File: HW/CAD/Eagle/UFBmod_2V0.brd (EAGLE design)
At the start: 98.4 x 89.5 mm, 93 parts, among them T0551 MMBT2222, U0501 MIDAS_MCCOG21605B6W-FPTLWI, U0601 MAX5217, U0701 AT86RF215-ZU, U0711 ASVTX-13-D-26.000MHZ-I05-T, U0811 PE4259, U0821 RFX1010, U0881 B39871B3440U410, X0891 ANTENNATINY, X0895 ANTENNATINY, X1011 TTE_EN11-HSM, X1211 MOLEX 105017-0001, X1221 PHOENIX_1990067_1X8X2MM50_PTS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, X1222 PHOENIX_1990067_1X8X2MM50_PTS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, X1223 PHOENIX_1990067_1X8X2MM50_PTS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

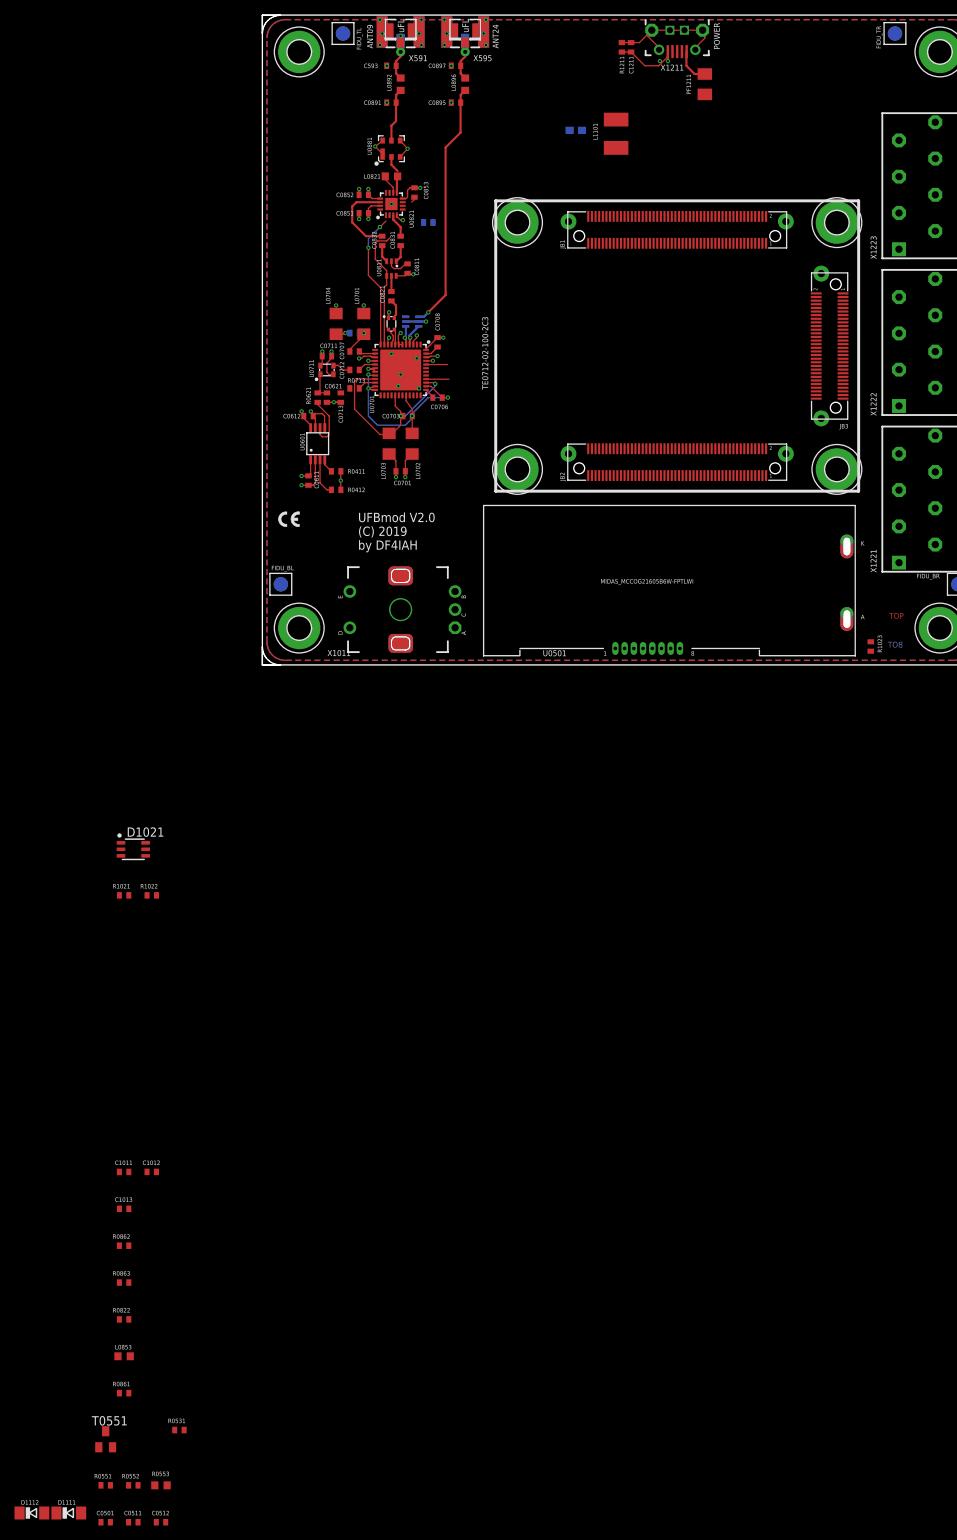
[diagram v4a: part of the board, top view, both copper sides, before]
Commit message: HW_2V0 - HW/CAD/Eagle - TPS53353 added
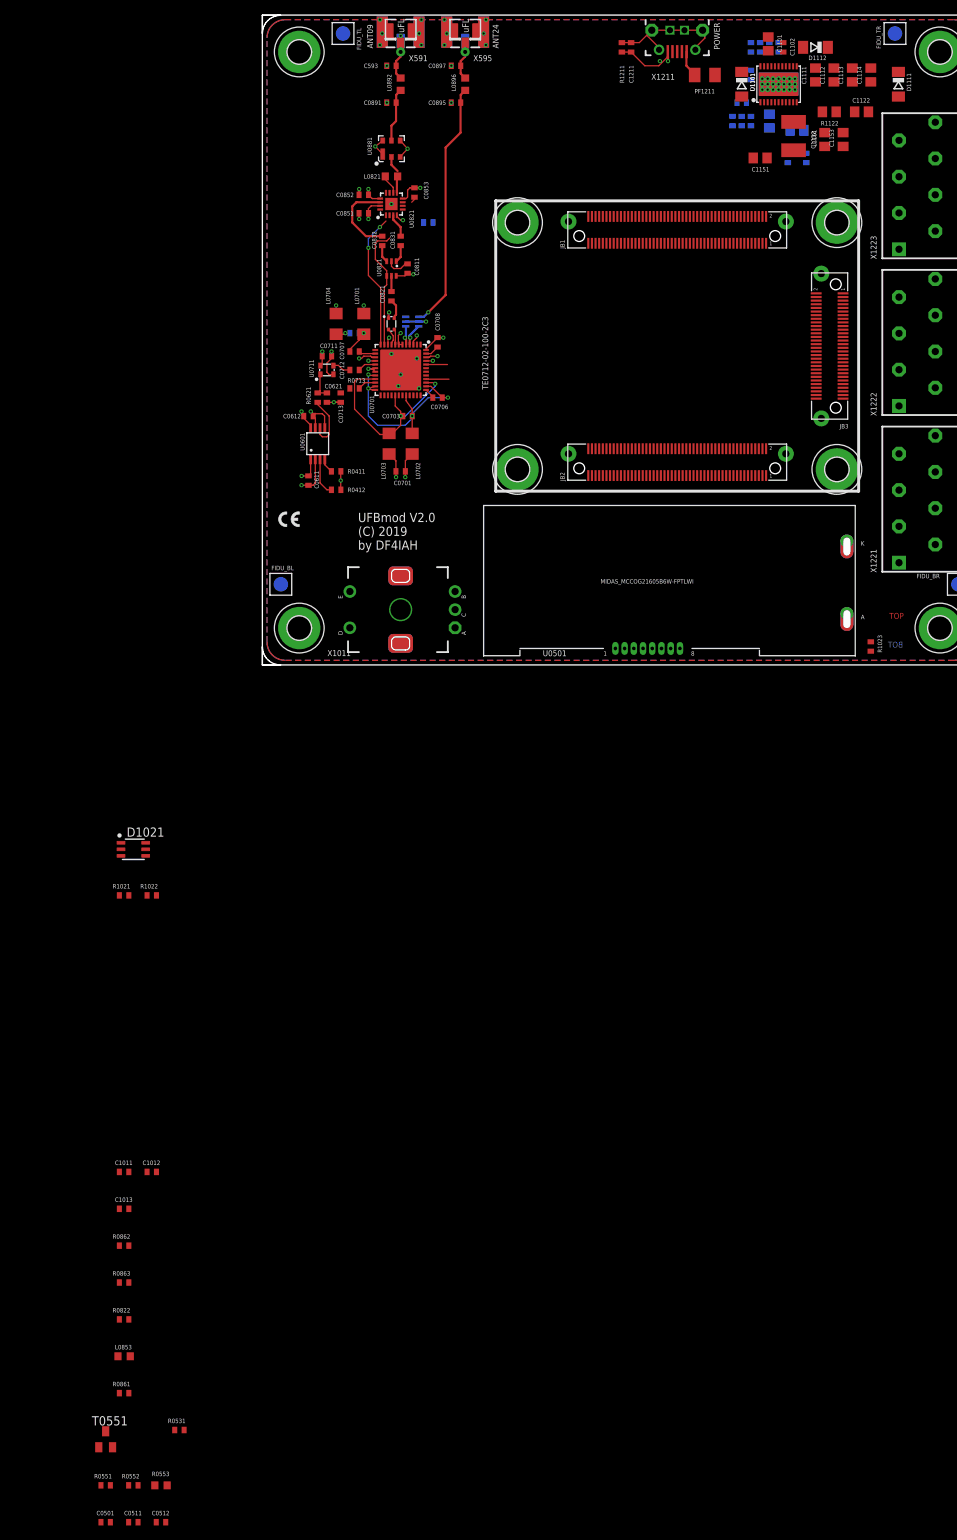
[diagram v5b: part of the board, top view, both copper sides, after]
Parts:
- removed C1121: 22uF, df4iah_rcl:C0603
- added C1101: 4.7uF, df4iah_rcl:C0805
- added C1102: 1uF, df4iah_rcl:C0402
- added C1108: 100nF, df4iah_rcl:C0805
- added C1111, C1112, C1113, C1114: 22uF, df4iah_rcl:C0805
- added C1122: N/A, df4iah_rcl:C0805
- added C1131: 100nF, df4iah_rcl:C0402
- added C1132: 1nF, df4iah_rcl:C0402
- added C1151, C1152, C1153: 100uF, df4iah_rcl:C0805
- added D1161: CRS08, df4iah_diode:SOD80C
- added R1101: 10kR, df4iah_rcl:R0402
- added R1102: 48.7kR, df4iah_rcl:R0402
- added R1103: 187kR, df4iah_rcl:R0402
- added R1104: N/A, df4iah_rcl:R0402
- added R1105: 110kR, df4iah_rcl:R0402
- added R1106: 200kR, df4iah_rcl:R0402
- added R1107: 100kR, df4iah_rcl:R0402
- added R1108: 2R, df4iah_rcl:R0805
- added R1122: N/A, df4iah_rcl:R0805
- added R1131: 3.01kR, df4iah_rcl:R0402
- added R1161: 220kR, df4iah_rcl:R0402
- added U1101: TPS53353, df4iah_powersupply:DQP-22
- moved D1112 229.0 mm to (76.2, 85.1), turned to 180 degrees
- moved D1111 227.6 mm to (87.6, 80.0), turned to 270 degrees
- moved L1101 24.4 mm to (73.2, 72.9), turned to 90 degrees
- moved PF1211 1.27 mm to (61.0, 81.3), turned to 180 degrees
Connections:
- removed net PMIC3V3_SW: L1101.2
- removed net VIN_REG: D1111.C, D1112.C
- new net +3V5: C1131.1, C1151.1, C1152.1, C1153.1, L1101.1, R1102.2, R1104.1
- new net TPS_COR: C1131.2, C1132.1, R1131.2
- new net TPS_EN: D1161.A, R1161.1, U1101.2
- new net TPS_LL: C1108.1, L1101.2, R1122.2, R1131.1, U1101.10, U1101.11, U1101.6, U1101.7, U1101.8, U1101.9
- new net TPS_LL_RC: C1122.1, R1122.1
- new net TPS_MODE: R1106.2, U1101.20
- new net TPS_PGOOD: R1107.1, U1101.3
- new net TPS_RF: R1103.2, R1104.2, U1101.22
- new net TPS_TRIP: R1105.2, U1101.21
- new net TPS_VBST: R1108.1, U1101.4
- new net TPS_VBST_R: C1108.2, R1108.2
- new net TPS_VFB: C1132.2, R1101.2, R1102.1, U1101.1
- new net TPS_VIN: C1101.2, C1111.2, C1112.2, C1113.2, C1114.2, D1111.C, D1112.C, R1161.2, U1101.12, U1101.13, U1101.14, U1101.15, U1101.16, U1101.17, U1101.19
- new net TPS_VREG: C1102.2, D1161.C, R1107.2, U1101.18
- net +3V3: no longer C1121.1, L1101.1
- net GND: now also C1101.1, C1102.1, C1111.1, C1112.1, C1113.1, C1114.1, C1122.2, C1151.2, C1152.2, C1153.2, R1101.1, R1103.1, R1105.1, R1106.1, U1101.23, U1101.24, U1101.P$1, U1101.P$10, U1101.P$11, U1101.P$12, U1101.P$13, U1101.P$14, U1101.P$15, U1101.P$16, U1101.P$17, U1101.P$18, U1101.P$19, U1101.P$2, U1101.P$20, U1101.P$21, U1101.P$3, U1101.P$4, U1101.P$5, U1101.P$6, U1101.P$7, U1101.P$8, U1101.P$9; no longer C1121.2
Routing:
- net USB_VBUS: track 4.97 -> 3.70 mm

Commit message: HW_2V0 - HW/CAD/Eagle - work of the day
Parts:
- added C1201, C1221: 10uF, df4iah_rcl:C0603
- added L1211: 4.7uH, df4iah_rcl:L2520
- added R0001, R0002, R0003, R0532: 1kR, df4iah_rcl:R0402
- added R0211: 0R, df4iah_rcl:R0402
- added R0212: N/A, df4iah_rcl:R0402
- added U1211: TPS62745DSSR, df4iah_powersupply:WSON-12
- C1011, C1012, C1013: value 1nF -> 100nF
- moved R0553 160.3 mm to (74.9, 20.3), flipped to the bottom, turned to 270 degrees
- moved R0551 158.5 mm to (74.9, 12.7), flipped to the bottom, turned to 90 degrees
- moved R0552 157.8 mm to (72.4, 16.5), flipped to the bottom, turned to 90 degrees
- moved T0551 157.3 mm to (76.2, 16.5), flipped to the bottom, turned to 90 degrees
- moved C0501 144.3 mm to (53.5, 5.08), flipped to the bottom, turned to 180 degrees
- moved C0511 140.8 mm to (50.3, 5.08), flipped to the bottom
- moved C0512 137.5 mm to (47.1, 5.08), flipped to the bottom
- moved R0531 129.8 mm to (56.7, 5.08), flipped to the bottom, turned to 180 degrees
- moved C1012 90.6 mm to (28.7, 9.37), flipped to the bottom, turned to 270 degrees
- moved C1011 89.5 mm to (28.7, 5.87), flipped to the bottom, turned to 90 degrees
- moved C1013 88.4 mm to (12.1, 7.78), flipped to the bottom, turned to 270 degrees
- moved R1021 68.5 mm to (25.4, 20.3), flipped to the bottom, turned to 90 degrees
- moved R1022 66.8 mm to (26.7, 20.3), flipped to the bottom, turned to 90 degrees
- moved D1021 61.1 mm to (26.7, 16.5), turned to 180 degrees
- moved R1023 58.6 mm to (27.9, 20.3), flipped to the bottom, turned to 90 degrees
- renumbered C1211 to C1311, H1311 to H1411, H1312 to H1412, H1313 to H1413, H1314 to H1414, PF1211 to PF1311, R1211 to R1311, X1211 to X1311, X1221 to X1321, X1222 to X1322, X1223 to X1323
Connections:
- net LCD_BL_PWM renamed FPGA_LCD_BL_PWM
- net LED_B1 renamed FPGA_LED_RGB_BLUE
- net LED_B_B renamed LCD_BL_B
- net LED_B_R1 renamed LED_RGB_BLUE
- net LED_G1 renamed FPGA_LED_RGB_GREEN
- net LED_G_R1 renamed LED_RGB_GREEN
- net LED_R1 renamed FPGA_LED_RGB_RED
- net LED_R_R1 renamed LED_RGB_RED
- removed net ROT_I_R: C1011.1, X1011.A
- removed net ROT_Q_R: C1012.1, X1011.B
- removed net U3V3IN: JB1.14, JB1.16
- removed net VCCIO15: JB2.10, JB2.8
- removed net VCCIO16: JB1.10, JB1.12
- removed net VDD: U0501.4
- removed net VIN: JB1.2, JB1.4, JB1.6, JB2.1, JB2.3, JB2.5, JB2.7
- removed net VSS: U0501.5
- new net +1V5: JB2.20
- new net +1V8: JB1.40, R0212.1
- new net +2V5: C1221.1, L1211.1, R0211.1, U1211.5
- new net FPGA_ETH_RD_N: JB1.11
- new net FPGA_ETH_RD_P: JB1.9
- new net FPGA_ETH_TD_N: JB1.5
- new net FPGA_ETH_TD_P: JB1.3
- new net FPGA_LCD_NRST: R0532.1
- new net FPGA_ROT_I: R0001.2
- new net FPGA_ROT_P: R0003.2
- new net FPGA_ROT_Q: R0002.2
- new net PMIC3V3_SW: L1211.2, U1211.2
- new net ROT_I: C1011.1, R0001.1, X1011.A
- new net ROT_Q: C1012.1, R0002.1, X1011.B
- net +3V3: now also JB1.10, JB1.12, JB1.13, JB2.10, JB2.11, JB2.8, JB2.9, U0501.4
- net +3V5: now also C1201.1, JB1.14, JB1.16, JB1.2, JB1.4, JB1.6, JB2.1, JB2.3, JB2.5, JB2.7, U1211.1, U1211.10, U1211.11, U1211.12, U1211.9
- net FPGA_I2C_SCL: now also U0501.7
- net FPGA_I2C_SDA: now also U0501.6
- net GND: now also C1201.2, C1221.2, U0501.5, U1211.13, U1211.14, U1211.3, U1211.4, U1211.8, U1211.G1, U1211.G2, U1211.G3, X1323.8
- net LCD_CAP1N: now also U0501.2
- net LCD_CAP1P: now also U0501.3
- net LCD_NRST: now also R0532.2, U0501.8
- net LCD_VOUT: now also U0501.1
- net ROT_P: now also R0003.1
- net VCCIO13: now also R0211.2, R0212.2
- net VIN_PWR: now also X1323.7
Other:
- board text added: "12V"
- board text added: "GND"

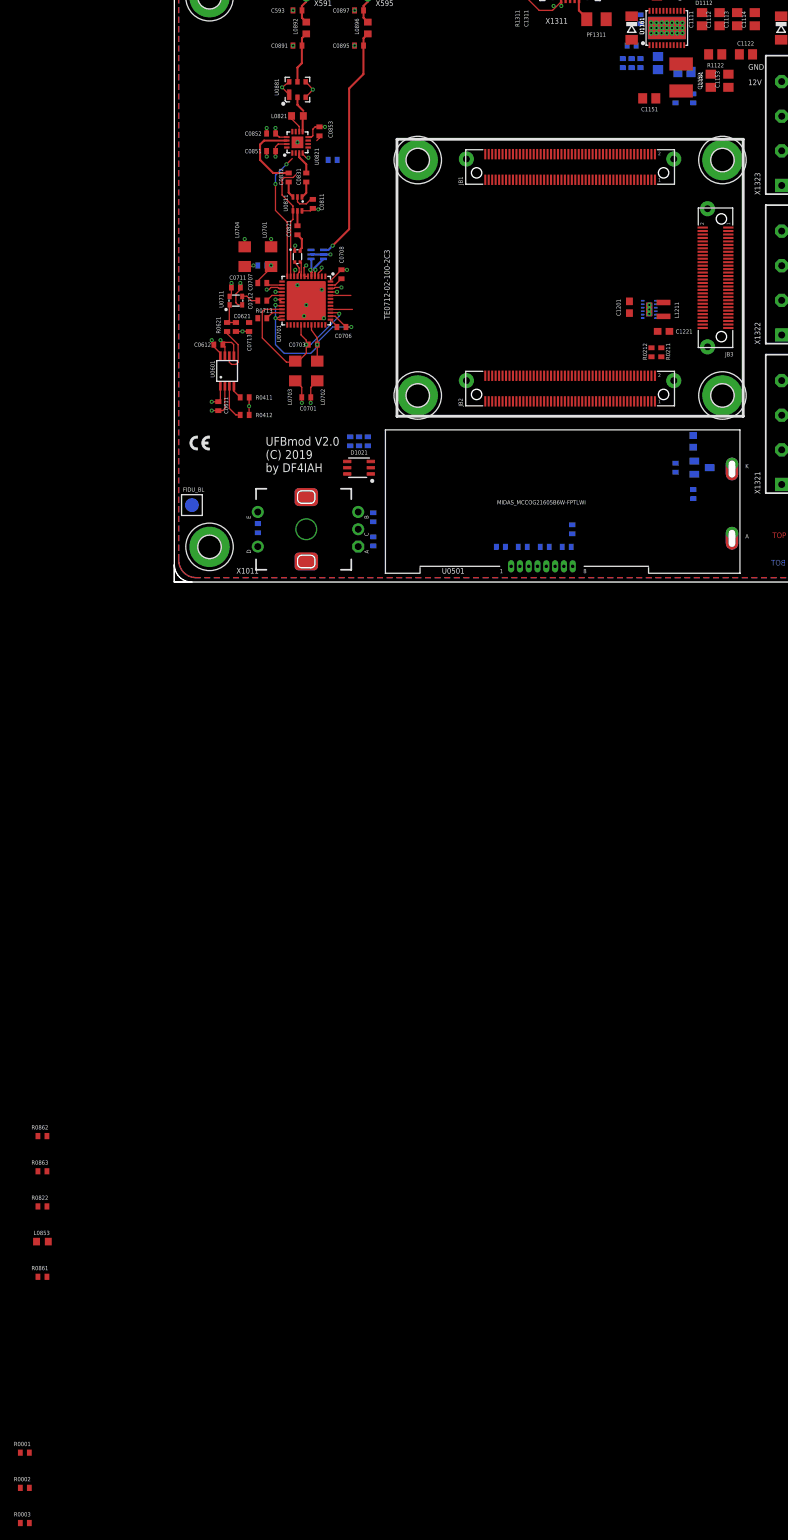
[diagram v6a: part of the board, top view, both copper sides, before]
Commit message: HW_2V0 - HW/CAD/Eagle - XILINX-JTAG header added, some more placements done
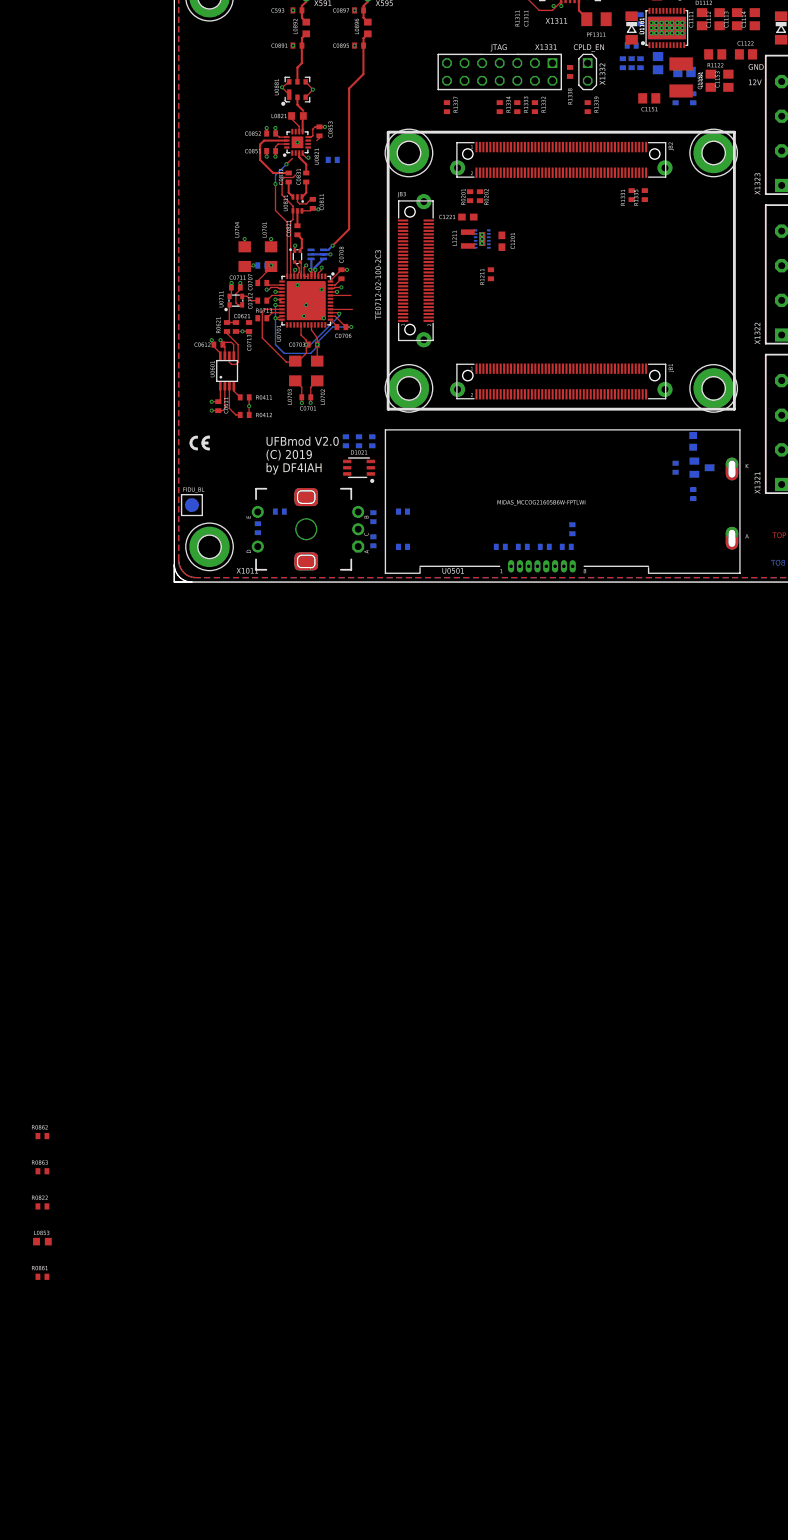
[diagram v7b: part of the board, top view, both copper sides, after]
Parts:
- removed R0001, R0002, R0003: 1kR, df4iah_rcl:R0402
- removed R0211: 0R, df4iah_rcl:R0402
- removed R0212: N/A, df4iah_rcl:R0402
- added R0201: 0R, df4iah_rcl:R0402
- added R0202: N/A, df4iah_rcl:R0402
- added R1011, R1012, R1013, R1331: 1kR, df4iah_rcl:R0402
- added R1211, R1338: 10kR, df4iah_rcl:R0402
- added R1332, R1333, R1334, R1335, R1337, R1339: 100R, df4iah_rcl:R0402
- added X1331: (no value), df4iah_connector:2X07_SHROUDED_JTAG_XILINX
- added X1332: (no value), df4iah_connector:1X02
- R1101: value 10kR -> 10kR 0%5
- R1102: value 48.7kR -> 45.3kR 0%5
- moved HB_354 57.2 mm to (33.9, 62.0), turned to 180 degrees
- moved HB_353 56.0 mm to (33.9, 28.0), turned to 180 degrees
- moved HB_352 55.2 mm to (77.9, 62.0), turned to 180 degrees
- moved HB_351 54.0 mm to (77.9, 28.0), turned to 180 degrees
- moved JB3 43.3 mm to (34.9, 45.0), turned to 270 degrees
- moved JB2 33.0 mm to (55.9, 61.0), turned to 180 degrees
- moved C1221 32.7 mm to (42.4, 52.7), turned to 0 degrees
- moved JB1 31.0 mm to (55.9, 29.0), turned to 180 degrees
- moved L1211 30.0 mm to (42.4, 49.5), turned to 270 degrees
- moved U1211 26.2 mm to (44.5, 49.5), turned to 180 degrees
- moved C1201 20.7 mm to (47.3, 49.2), turned to 90 degrees
- moved R1021 0.63 mm to (24.8, 20.3)
- moved R1023 0.63 mm to (28.6, 20.3)
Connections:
- net +1V5 renamed U1V5
- removed net +1V8: JB1.40, R0212.1
- removed net +3V5: C1131.1, C1151.1, C1152.1, C1153.1, C1201.1, JB1.14, JB1.16, JB1.2, JB1.4, JB1.6, JB2.1, JB2.3, JB2.5, JB2.7, L1101.1, R1102.2, R1104.1, U1211.1, U1211.10, U1211.11, U1211.12, U1211.9
- new net FPGA_JTAGEN: JB1.90, R1339.2
- new net FPGA_SRST: JB2.90, R1337.2
- new net FPGA_TCK: JB2.100, R1333.2
- new net FPGA_TDI: JB2.96, R1335.2
- new net FPGA_TDO: JB2.98, R1334.2
- new net FPGA_TMS: JB2.94, R1332.2
- new net JC_SRST: R1337.1, X1331.14
- new net JC_TCK: R1333.1, X1331.6
- new net JC_TDI: R1335.1, X1331.10
- new net JC_TDO: R1334.1, X1331.8
- new net JC_TMS: R1332.1, X1331.4
- new net JC_VCCO_0: R1331.1, X1331.2
- new net JTAG_CPLD_EN: R1338.1, R1339.1, X1332.2
- new net TPS2_EN: R1211.2, U1211.12
- new net U1V8: JB1.40, R0202.1
- new net U3V3: JB1.10, JB1.12, JB1.13, JB2.10, JB2.11, JB2.8, JB2.9, R1211.1
- new net U3V3_JTAGREF: JB2.92, R1331.2
- new net USB_D_M: X1311.D-
- new net USB_D_P: X1311.D+
- new net USB_ID: X1311.ID
- net +2V5: now also R0201.1; no longer R0211.1
- net +3V3: now also C1131.1, C1151.1, C1152.1, C1153.1, C1201.1, JB1.14, JB1.16, JB1.2, JB1.4, JB1.6, JB2.1, JB2.3, JB2.5, JB2.7, L1101.1, R1102.2, R1104.1, U1211.1, U1211.10, U1211.11, U1211.9, X1332.1; no longer JB1.10, JB1.12, JB1.13, JB2.10, JB2.11, JB2.8, JB2.9
- net FPGA_ROT_I: now also R1011.2; no longer R0001.2
- net FPGA_ROT_P: now also R1013.2; no longer R0003.2
- net FPGA_ROT_Q: now also R1012.2; no longer R0002.2
- net FPGA_TRX_CLKO: now also JB1.76
- net GND: now also R1338.2, X1331.1, X1331.11, X1331.13, X1331.3, X1331.5, X1331.7, X1331.9
- net ROT_I: now also R1011.1; no longer R0001.1
- net ROT_P: now also R1013.1; no longer R0003.1
- net ROT_Q: now also R1012.1; no longer R0002.1
- net TRX_RXCLK_N: now also JB1.22
- net TRX_RXCLK_P: now also JB1.24
- net TRX_RXD09_N: now also JB1.20
- net TRX_RXD09_P: now also JB1.18
- net TRX_RXD24_N: now also JB1.26
- net TRX_RXD24_P: now also JB1.28
- net TRX_TXCLK_N: now also JB1.15
- net TRX_TXCLK_P: now also JB1.17
- net TRX_TXD_N: now also JB1.21
- net TRX_TXD_P: now also JB1.23
- net VCCIO13: now also R0201.2, R0202.2; no longer R0211.2, R0212.2
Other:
- board text added: "CPLD_EN"
- board text added: "JTAG"
